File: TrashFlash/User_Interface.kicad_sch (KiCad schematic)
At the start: 14 parts, among them IC7 LP5024RSMR

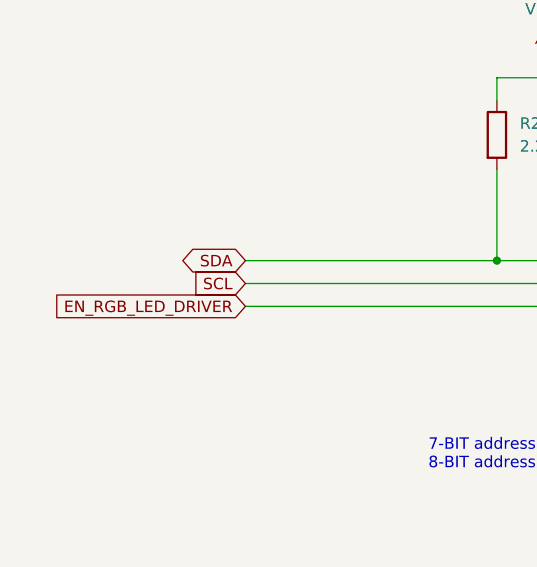
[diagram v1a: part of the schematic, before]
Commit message: Added Battery Management
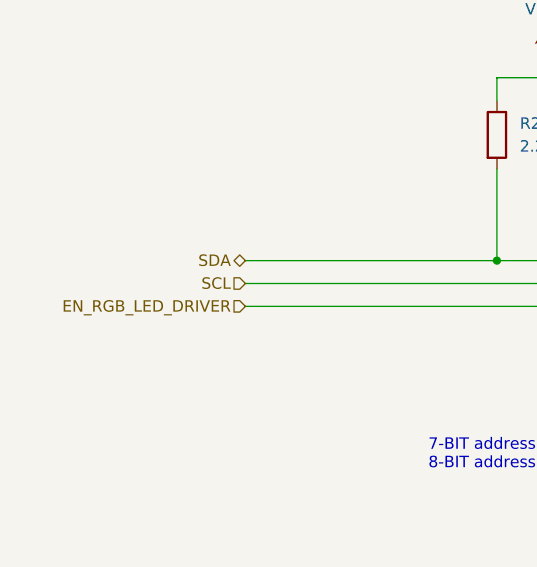
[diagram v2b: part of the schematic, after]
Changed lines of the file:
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@@
 		)
 	)
-	(global_label "SDA"
-		(shape bidirectional)
-		(at 76.2 60.96 180)
-		(fields_autoplaced yes)
+	(hierarchical_label "SCL"
+		(shape input)
+		(at 76.2 63.5 180)
 		(effects
 			(font
@@
 			(justify right)
 		)
-		(property "Intersheetrefs" "${INTERSHEET_REFS}"
-			(at 68.5354 60.96 0)
-			(effects
-				(font
-					(size 1.27 1.27)
-				)
-				(justify right)
-				(hide yes)
-			)
-		)
 	)
-	(global_label "EN_RGB_LED_DRIVER"
-		(shape input)
-		(at 76.2 66.04 180)
-		(fields_autoplaced yes)
+	(hierarchical_label "SDA"
+		(shape bidirectional)
+		(at 76.2 60.96 180)
 		(effects
 			(font
@@
 			(justify right)
 		)
-		(property "Intersheetrefs" "${INTERSHEET_REFS}"
-			(at 53.923 66.04 0)
-			(effects
-				(font
-					(size 1.27 1.27)
-				)
-				(justify right)
-				(hide yes)
-			)
-		)
 	)
-	(global_label "SCL"
+	(hierarchical_label "EN_RGB_LED_DRIVER"
 		(shape input)
-		(at 76.2 63.5 180)
-		(fields_autoplaced yes)
+		(at 76.2 66.04 180)
 		(effects
 			(font
@@
 			(justify right)
 		)
-		(property "Intersheetrefs" "${INTERSHEET_REFS}"
-			(at 69.7072 63.5 0)
-			(effects
-				(font
-					(size 1.27 1.27)
-				)
-				(justify right)
-				(hide yes)
-			)
-		)
 	)

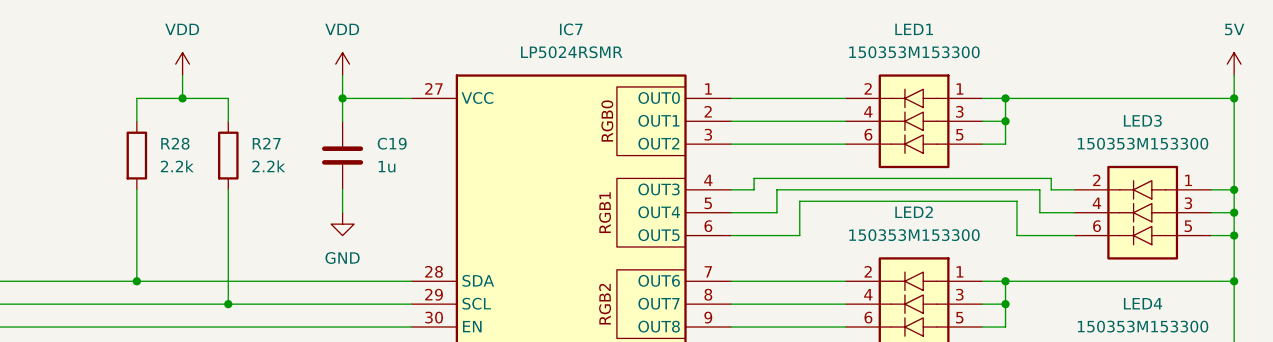
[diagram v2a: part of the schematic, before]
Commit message: Added USB and powernets
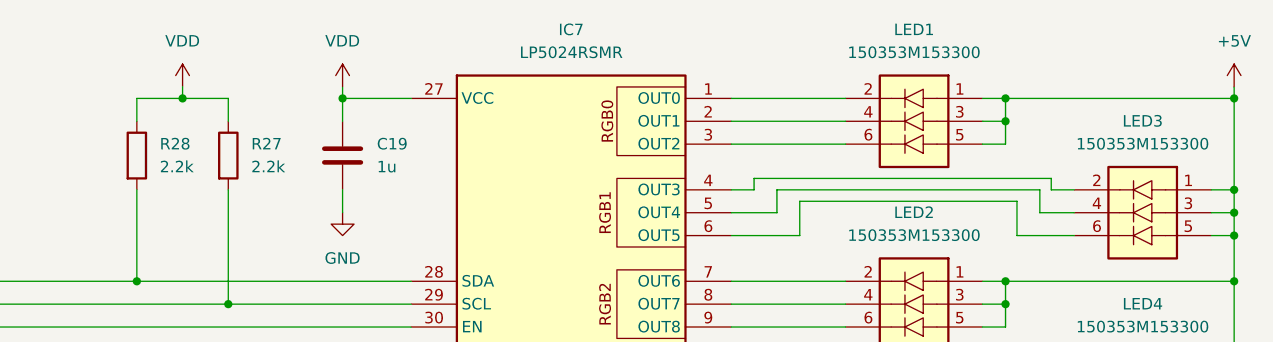
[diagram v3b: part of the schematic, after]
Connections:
- net 5V renamed +5V
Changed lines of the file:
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@@
 	(wire
 		(pts
-			(xy 127 38.1) (xy 127 40.64)
+			(xy 127 39.37) (xy 127 40.64)
 		)
 		(stroke
@@
 	(wire
 		(pts
-			(xy 226.06 38.1) (xy 226.06 40.64)
+			(xy 226.06 39.37) (xy 226.06 40.64)
 		)
 		(stroke
@@
 	(wire
 		(pts
-			(xy 109.22 38.1) (xy 109.22 40.64)
+			(xy 109.22 39.37) (xy 109.22 40.64)
 		)
 		(stroke
@@
 	)
 	(symbol
-		(lib_id "power:+3V3")
-		(at 226.06 38.1 0)
-		(unit 1)
-		(exclude_from_sim no)
-		(in_bom yes)
-		(on_board yes)
-		(dnp no)
-		(fields_autoplaced yes)
-		(property "Reference" "#PWR033"
-			(at 226.06 41.91 0)
-			(effects
-				(font
-					(size 1.27 1.27)
-				)
-				(hide yes)
-			)
-		)
-		(property "Value" "5V"
-			(at 226.06 33.02 0)
-			(effects
-				(font
-					(size 1.27 1.27)
-				)
-			)
-		)
-		(property "Footprint" ""
-			(at 226.06 38.1 0)
-			(effects
-				(font
-					(size 1.27 1.27)
-				)
-				(hide yes)
-			)
-		)
-		(property "Datasheet" ""
-			(at 226.06 38.1 0)
-			(effects
-				(font
-					(size 1.27 1.27)
-				)
-				(hide yes)
-			)
-		)
-		(property "Description" "Power symbol creates a global label with name \"+3V3\""
-			(at 226.06 38.1 0)
-			(effects
-				(font
-					(size 1.27 1.27)
-				)
-				(hide yes)
-			)
-		)
-		(pin "1"
-		)
-		(instances
-			(project ""
-				(path "/256082dc-9c82-41ae-bfb7-0b4bd4121c78/fa02bcf9-bdc6-4000-b431-14bacede6ea5"
-					(reference "#PWR033")
-					(unit 1)
-				)
-			)
-		)
-	)
-	(symbol
 		(lib_id "TrashFlash:LP5024RSMR")
 		(at 139.7 38.1 0)
@@
 	)
 	(symbol
+		(lib_id "power:+5V")
+		(at 226.06 39.37 0)
+		(unit 1)
+		(exclude_from_sim no)
+		(in_bom yes)
+		(on_board yes)
+		(dnp no)
+		(fields_autoplaced yes)
+		(property "Reference" "#PWR031"
+			(at 226.06 43.18 0)
+			(effects
+				(font
+					(size 1.27 1.27)
+				)
+				(hide yes)
+			)
+		)
+		(property "Value" "+5V"
+			(at 226.06 34.29 0)
+			(effects
+				(font
+					(size 1.27 1.27)
+				)
+			)
+		)
+		(property "Footprint" ""
+			(at 226.06 39.37 0)
+			(effects
+				(font
+					(size 1.27 1.27)
+				)
+				(hide yes)
+			)
+		)
+		(property "Datasheet" ""
+			(at 226.06 39.37 0)
+			(effects
+				(font
+					(size 1.27 1.27)
+				)
+				(hide yes)
+			)
+		)
+		(property "Description" "Power symbol creates a global label with name \"+5V\""
+			(at 226.06 39.37 0)
+			(effects
+				(font
+					(size 1.27 1.27)
+				)
+				(hide yes)
+			)
+		)
+		(pin "1"
+		)
+		(instances
+			(project ""
+				(path "/256082dc-9c82-41ae-bfb7-0b4bd4121c78/fa02bcf9-bdc6-4000-b431-14bacede6ea5"
+					(reference "#PWR031")
+					(unit 1)
+				)
+			)
+		)
+	)
+	(symbol
 		(lib_id "TrashFlash:150353M153300")
 		(at 233.68 111.76 0)
@@
 	(symbol
 		(lib_id "power:VDD")
-		(at 109.22 38.1 0)
+		(at 109.22 39.37 0)
 		(unit 1)
 		(exclude_from_sim no)
@@
 		(fields_autoplaced yes)
 		(property "Reference" "#PWR035"
-			(at 109.22 41.91 0)
+			(at 109.22 43.18 0)
 			(effects
 				(font
@@
 		)
 		(property "Value" "VDD"
-			(at 109.22 33.02 0)
+			(at 109.22 34.29 0)
 			(effects
 				(font
@@
 		)
 		(property "Footprint" ""
-			(at 109.22 38.1 0)
+			(at 109.22 39.37 0)
 			(effects
 				(font
@@
 		)
 		(property "Datasheet" ""
-			(at 109.22 38.1 0)
+			(at 109.22 39.37 0)
 			(effects
 				(font
@@
 		)
 		(property "Description" "Power symbol creates a global label with name \"VDD\""
-			(at 109.22 38.1 0)
+			(at 109.22 39.37 0)
 			(effects
 				(font
@@
 		)
 		(instances
-			(project ""
+			(project "TrashFlash"
 				(path "/256082dc-9c82-41ae-bfb7-0b4bd4121c78/fa02bcf9-bdc6-4000-b431-14bacede6ea5"
 					(reference "#PWR035")
-					(unit 1)
-				)
-			)
-		)
-	)
-	(symbol
-		(lib_id "power:VDD")
-		(at 127 38.1 0)
-		(unit 1)
-		(exclude_from_sim no)
-		(in_bom yes)
-		(on_board yes)
-		(dnp no)
-		(fields_autoplaced yes)
-		(property "Reference" "#PWR036"
-			(at 127 41.91 0)
-			(effects
-				(font
-					(size 1.27 1.27)
-				)
-				(hide yes)
-			)
-		)
-		(property "Value" "VDD"
-			(at 127 33.02 0)
-			(effects
-				(font
-					(size 1.27 1.27)
-				)
-			)
-		)
-		(property "Footprint" ""
-			(at 127 38.1 0)
-			(effects
-				(font
-					(size 1.27 1.27)
-				)
-				(hide yes)
-			)
-		)
-		(property "Datasheet" ""
-			(at 127 38.1 0)
-			(effects
-				(font
-					(size 1.27 1.27)
-				)
-				(hide yes)
-			)
-		)
-		(property "Description" "Power symbol creates a global label with name \"VDD\""
-			(at 127 38.1 0)
-			(effects
-				(font
-					(size 1.27 1.27)
-				)
-				(hide yes)
-			)
-		)
-		(pin "1"
-		)
-		(instances
-			(project ""
-				(path "/256082dc-9c82-41ae-bfb7-0b4bd4121c78/fa02bcf9-bdc6-4000-b431-14bacede6ea5"
-					(reference "#PWR036")
 					(unit 1)
 				)
@@
 					(unit 1)
 				)
+			)
+		)
+	)
+	(symbol
+		(lib_id "power:VDD")
+		(at 127 39.37 0)
+		(unit 1)
+		(exclude_from_sim no)
+		(in_bom yes)
+		(on_board yes)
+		(dnp no)
+		(fields_autoplaced yes)
+		(property "Reference" "#PWR036"
+			(at 127 43.18 0)
+			(effects
+				(font
+					(size 1.27 1.27)
+				)
+				(hide yes)
+			)
+		)
+		(property "Value" "VDD"
+			(at 127 34.29 0)
+			(effects
+				(font
+					(size 1.27 1.27)
+				)
+			)
+		)
+		(property "Footprint" ""
+			(at 127 39.37 0)
+			(effects
+				(font
+					(size 1.27 1.27)
+				)
+				(hide yes)
+			)
+		)
+		(property "Datasheet" ""
+			(at 127 39.37 0)
+			(effects
+				(font
+					(size 1.27 1.27)
+				)
+				(hide yes)
+			)
+		)
+		(property "Description" "Power symbol creates a global label with name \"VDD\""
+			(at 127 39.37 0)
+			(effects
+				(font
+					(size 1.27 1.27)
+				)
+				(hide yes)
+			)
+		)
+		(pin "1"
+		)
+		(instances
+			(project "TrashFlash"
+				(path "/256082dc-9c82-41ae-bfb7-0b4bd4121c78/fa02bcf9-bdc6-4000-b431-14bacede6ea5"
+					(reference "#PWR036")
+					(unit 1)
+				)

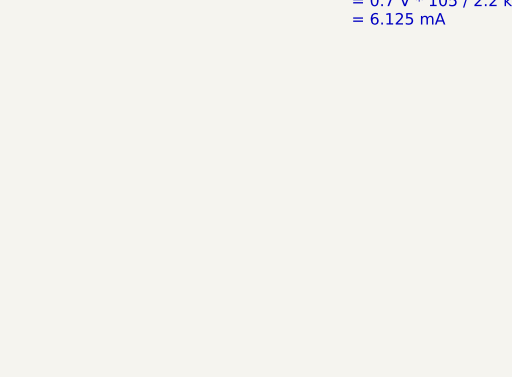
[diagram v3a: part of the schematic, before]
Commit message: Rotary encoder added + 3D stuff
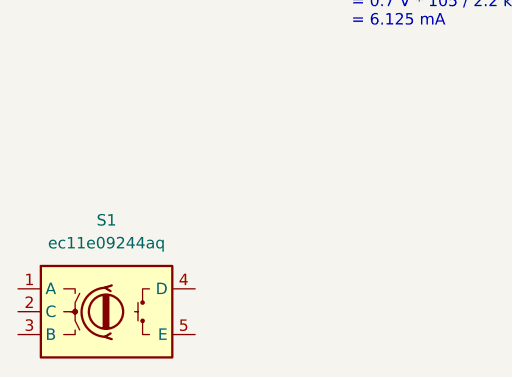
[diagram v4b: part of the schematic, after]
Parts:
- added S1: ec11e09244aq, TrashFlash:ec11e09244aq, symbol TrashFlash:ec11e09244aq
- C19, C20: footprint (none) -> Capacitor_SMD:C_0603_1608Metric
- IC7: footprint QFN40P400X400X100-33N-D -> TrashFlash:QFN40P400X400X100-33N-D
- LED1, LED2, LED3, LED4, LED5, LED6, LED7, LED8: footprint 150353M153300 -> TrashFlash:150353M153300
- R27, R28, R29: footprint (none) -> Resistor_SMD:R_0402_1005Metric
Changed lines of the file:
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@@
 			)
 		)
-		(property "Footprint" "150353M153300"
+		(property "Footprint" "TrashFlash:150353M153300"
 			(at 201.93 166.04 0)
 			(effects
@@
 			)
 		)
-		(property "Footprint" "150353M153300"
+		(property "Footprint" "TrashFlash:150353M153300"
 			(at 176.53 155.88 0)
 			(effects
@@
 				(path "/256082dc-9c82-41ae-bfb7-0b4bd4121c78/fa02bcf9-bdc6-4000-b431-14bacede6ea5"
 					(reference "LED2")
+					(unit 1)
+				)
+			)
+		)
+	)
+	(symbol
+		(lib_id "TrashFlash:ec11e09244aq")
+		(at 48.26 143.51 0)
+		(unit 1)
+		(exclude_from_sim no)
+		(in_bom yes)
+		(on_board yes)
+		(dnp no)
+		(fields_autoplaced yes)
+		(property "Reference" "S1"
+			(at 58.1025 135.89 0)
+			(effects
+				(font
+					(size 1.27 1.27)
+				)
+			)
+		)
+		(property "Value" "ec11e09244aq"
+			(at 58.1025 138.43 0)
+			(effects
+				(font
+					(size 1.27 1.27)
+				)
+			)
+		)
+		(property "Footprint" "TrashFlash:ec11e09244aq"
+			(at 48.26 143.51 0)
+			(effects
+				(font
+					(size 1.27 1.27)
+				)
+				(hide yes)
+			)
+		)
+		(property "Datasheet" "https://eu.mouser.com/datasheet/2/15/alps_alps-s-a0008379064-1-1733314.pdf"
+			(at 48.26 143.51 0)
+			(effects
+				(font
+					(size 1.27 1.27)
+				)
+				(hide yes)
+			)
+		)
+		(property "Description" ""
+			(at 48.26 143.51 0)
+			(effects
+				(font
+					(size 1.27 1.27)
+				)
+				(hide yes)
+			)
+		)
+		(pin "4"
+		)
+		(pin "2"
+		)
+		(pin "3"
+		)
+		(pin "5"
+		)
+		(pin "1"
+		)
+		(instances
+			(project ""
+				(path "/256082dc-9c82-41ae-bfb7-0b4bd4121c78/fa02bcf9-bdc6-4000-b431-14bacede6ea5"
+					(reference "S1")
 					(unit 1)
 				)
@@
 			)
 		)
-		(property "Footprint" "QFN40P400X400X100-33N-D"
+		(property "Footprint" "TrashFlash:QFN40P400X400X100-33N-D"
 			(at 138.43 127 0)
 			(effects
@@
 			)
 		)
-		(property "Footprint" "150353M153300"
+		(property "Footprint" "TrashFlash:150353M153300"
 			(at 201.93 186.36 0)
 			(effects
@@
 			)
 		)
-		(property "Footprint" "150353M153300"
+		(property "Footprint" "TrashFlash:150353M153300"
 			(at 176.53 176.2 0)
 			(effects
@@
 			)
 		)
-		(property "Footprint" ""
+		(property "Footprint" "Resistor_SMD:R_0402_1005Metric"
 			(at 102.362 46.99 90)
 			(effects
@@
 			)
 		)
-		(property "Footprint" ""
+		(property "Footprint" "Resistor_SMD:R_0402_1005Metric"
 			(at 112.522 111.76 90)
 			(effects
@@
 			)
 		)
-		(property "Footprint" "150353M153300"
+		(property "Footprint" "TrashFlash:150353M153300"
 			(at 201.93 145.72 0)
 			(effects
@@
 			)
 		)
-		(property "Footprint" "150353M153300"
+		(property "Footprint" "TrashFlash:150353M153300"
 			(at 201.93 206.68 0)
 			(effects
@@
 			)
 		)
-		(property "Footprint" "150353M153300"
+		(property "Footprint" "TrashFlash:150353M153300"
 			(at 176.53 135.56 0)
 			(effects
@@
 			)
 		)
-		(property "Footprint" ""
+		(property "Footprint" "Capacitor_SMD:C_0603_1608Metric"
 			(at 127.9652 50.8 0)
 			(effects
@@
 			)
 		)
-		(property "Footprint" ""
+		(property "Footprint" "Resistor_SMD:R_0402_1005Metric"
 			(at 112.522 46.99 90)
 			(effects
@@
 			)
 		)
-		(property "Footprint" "150353M153300"
+		(property "Footprint" "TrashFlash:150353M153300"
 			(at 176.53 196.52 0)
 			(effects
@@
 			)
 		)
-		(property "Footprint" ""
+		(property "Footprint" "Capacitor_SMD:C_0603_1608Metric"
 			(at 127.9652 115.57 0)
 			(effects

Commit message: Footprints 3D model fixed
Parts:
- IC7: footprint TrashFlash:QFN40P400X400X100-33N-D -> QFN40P400X400X100-33N-D
- LED1, LED2, LED3, LED4, LED5, LED6, LED7, LED8: footprint TrashFlash:150353M153300 -> 150353M153300
- S1: footprint TrashFlash:ec11e09244aq -> ec11e09244aq
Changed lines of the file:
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@@
 			)
 		)
-		(property "Footprint" "TrashFlash:150353M153300"
+		(property "Footprint" "150353M153300"
 			(at 201.93 166.04 0)
 			(effects
@@
 			)
 		)
-		(property "Footprint" "TrashFlash:150353M153300"
+		(property "Footprint" "150353M153300"
 			(at 176.53 155.88 0)
 			(effects
@@
 			)
 		)
-		(property "Footprint" "TrashFlash:ec11e09244aq"
+		(property "Footprint" "ec11e09244aq"
 			(at 48.26 143.51 0)
 			(effects
@@
 			)
 		)
-		(property "Footprint" "TrashFlash:QFN40P400X400X100-33N-D"
+		(property "Footprint" "QFN40P400X400X100-33N-D"
 			(at 138.43 127 0)
 			(effects
@@
 			)
 		)
-		(property "Footprint" "TrashFlash:150353M153300"
+		(property "Footprint" "150353M153300"
 			(at 201.93 186.36 0)
 			(effects
@@
 			)
 		)
-		(property "Footprint" "TrashFlash:150353M153300"
+		(property "Footprint" "150353M153300"
 			(at 176.53 176.2 0)
 			(effects
@@
 			)
 		)
-		(property "Footprint" "TrashFlash:150353M153300"
+		(property "Footprint" "150353M153300"
 			(at 201.93 145.72 0)
 			(effects
@@
 			)
 		)
-		(property "Footprint" "TrashFlash:150353M153300"
+		(property "Footprint" "150353M153300"
 			(at 201.93 206.68 0)
 			(effects
@@
 			)
 		)
-		(property "Footprint" "TrashFlash:150353M153300"
+		(property "Footprint" "150353M153300"
 			(at 176.53 135.56 0)
 			(effects
@@
 			)
 		)
-		(property "Footprint" "TrashFlash:150353M153300"
+		(property "Footprint" "150353M153300"
 			(at 176.53 196.52 0)
 			(effects
